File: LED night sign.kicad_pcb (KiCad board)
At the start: 2 copper layers, 42.9 x 36.7 mm, 39 parts, among them Q1 MOSFET-NCH-2N7002PW, Q2 BC817, U1 ATtiny85-20M, U2 APDS-9301

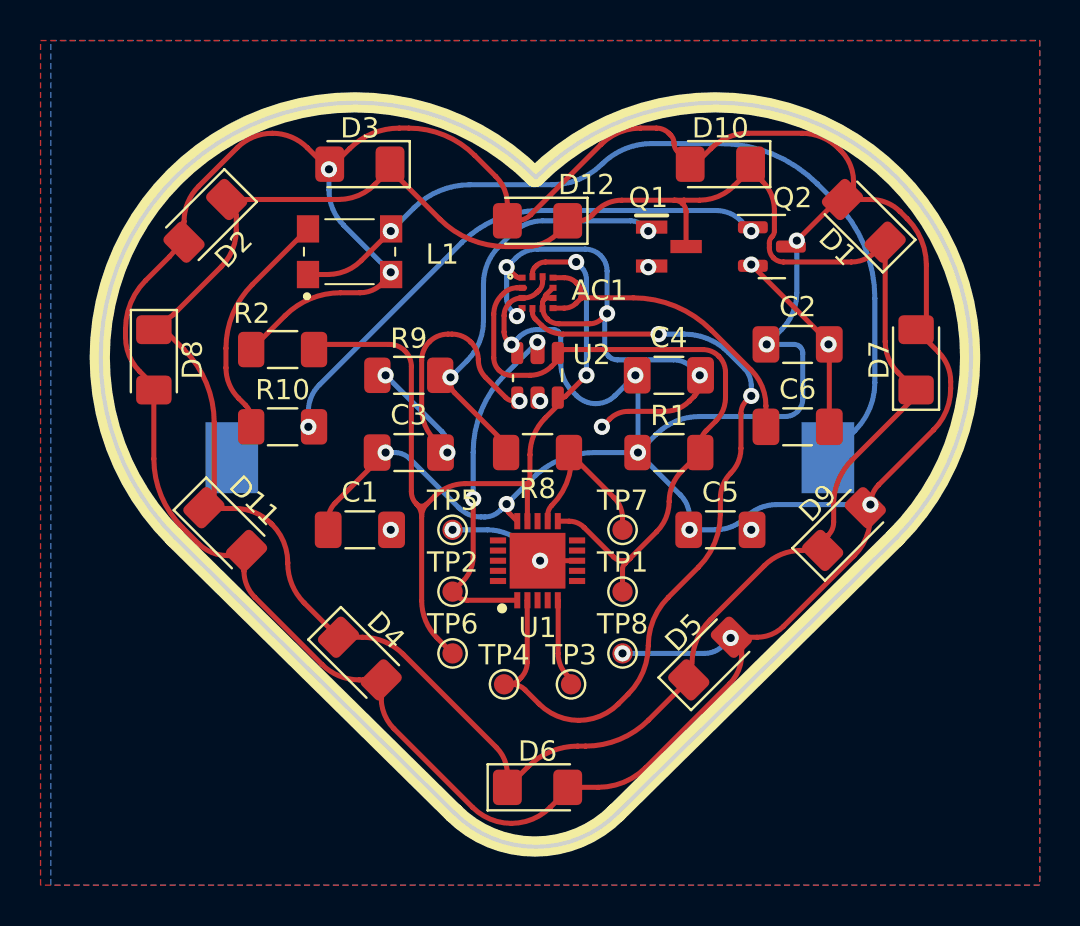
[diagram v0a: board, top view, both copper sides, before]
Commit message: changed ic for light sensing
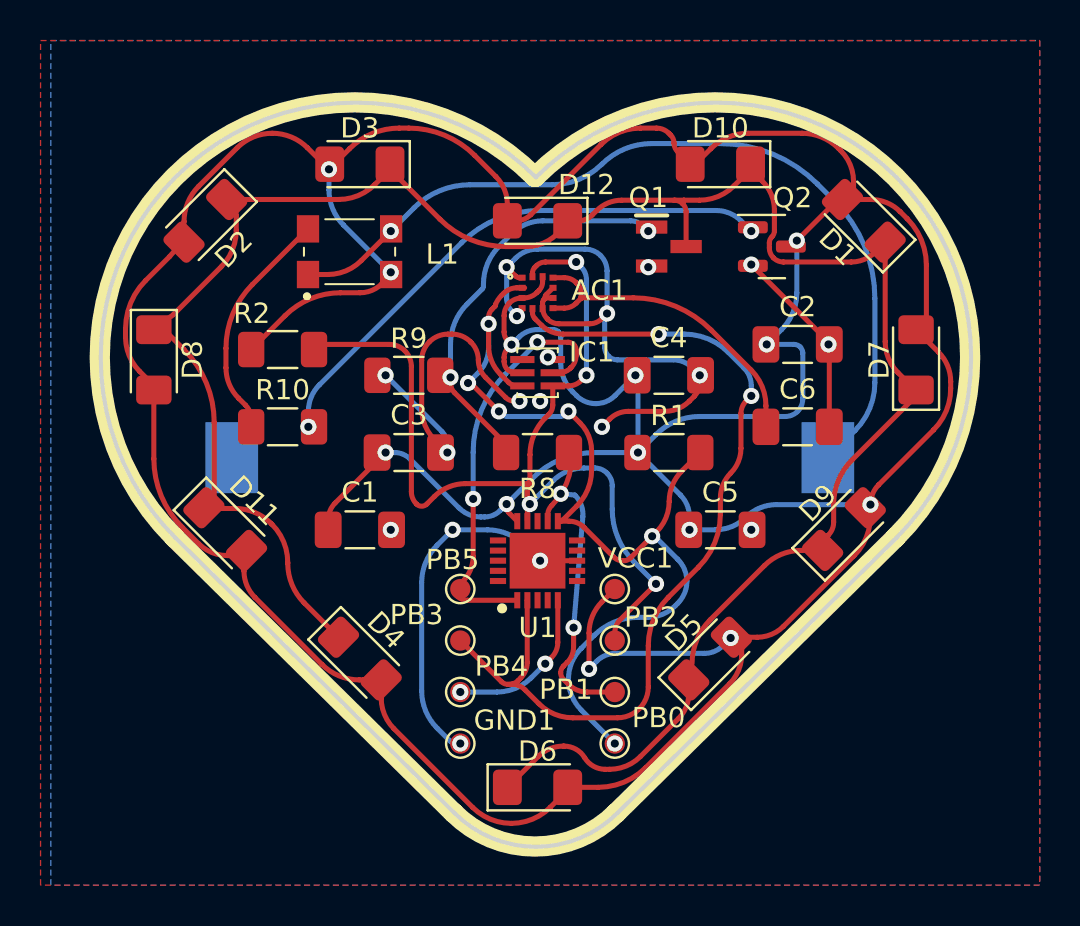
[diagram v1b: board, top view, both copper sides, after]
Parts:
- removed TP1, TP4: pb0, TestPoint:TestPoint_Pad_D1.0mm
- removed TP2: pb5, TestPoint:TestPoint_Pad_D1.0mm
- removed TP3: pb4, TestPoint:TestPoint_Pad_D1.0mm
- removed TP5: gnd, TestPoint:TestPoint_Pad_D1.0mm
- removed TP6: pb2, TestPoint:TestPoint_Pad_D1.0mm
- removed TP7: pb1, TestPoint:TestPoint_Pad_D1.0mm
- removed TP8: vcc, TestPoint:TestPoint_Pad_D1.0mm
- removed U2: APDS-9301, OptoDevice:Broadcom_APDS-9301
- added GND1: gnd, TestPoint:TestPoint_Pad_D1.0mm, F.Cu at (146.2, 117.5)
- added IC1: TSL25911FN, SamacSys_Parts:TSL25911FN, F.Cu at (150.0, 99.2)
- added PB0: pb0, TestPoint:TestPoint_Pad_D1.0mm, F.Cu at (153.8, 117.5)
- added PB1: pb1, TestPoint:TestPoint_Pad_D1.0mm, F.Cu at (153.8, 114.9)
- added PB2: pb2, TestPoint:TestPoint_Pad_D1.0mm, F.Cu at (153.8, 112.4)
- added PB3: pb0, TestPoint:TestPoint_Pad_D1.0mm, F.Cu at (146.2, 112.4)
- added PB4: pb4, TestPoint:TestPoint_Pad_D1.0mm, F.Cu at (146.2, 114.9)
- added PB5: pb5, TestPoint:TestPoint_Pad_D1.0mm, F.Cu at (146.2, 109.9)
- added VCC1: vcc, TestPoint:TestPoint_Pad_D1.0mm, F.Cu at (153.8, 109.9)
- moved G*** 1.16 mm to (149.7, 116.1)
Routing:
- net PB0/SDA/MOSI: track 34.6 -> 47.7 mm, vias 0 -> 6
- net GND: track 64.1 -> 76.1 mm, vias 16 -> 18
- net Net-(D1-Pad1): track 118.6 -> 109.0 mm
- net CTRLLED: track 8.17 -> 16.3 mm, vias 0 -> 2
- net JouleThiefPWR: track 225.3 -> 233.2 mm
- net PB2/SCL/SCK: track 43.7 -> 50.0 mm, vias 2 -> 4
- net INTL: track 16.9 -> 20.9 mm
- net INTM: track 41.1 -> 45.1 mm
- net PB4: track 4.45 -> 7.98 mm, vias 0 -> 2
